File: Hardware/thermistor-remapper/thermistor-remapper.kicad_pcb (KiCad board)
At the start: 2 copper layers, 40 x 56.5 mm, 31 parts, among them Q1 2N7002, Q2 2N7002, Q3 2N7002, Q4 2N7002, Q5 2N7002, Q6 2N7002, Q7 2N7002, U1 MX8500-8.5-04P-BK01-CU-S-A, U2 XL1509-5.0E1

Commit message: Completed prototype
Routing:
- net VDD: track 21.3 -> 53.6 mm, vias 0 -> 1
- net BIT1: track 0.00 -> 8.69 mm
- net BIT2: track 0.00 -> 8.26 mm
- net BIT3: track 0.00 -> 7.51 mm
- net BIT4: track 0.00 -> 6.90 mm
- net BIT5: track 0.00 -> 6.60 mm
- net BIT6: track 0.00 -> 6.41 mm
- net BIT7: track 0.00 -> 6.22 mm
- added copper zone on B.Cu, net GND
- added copper zone on F.Cu, net GND
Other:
- board size 40 x 56.5 mm -> 40 x 57 mm

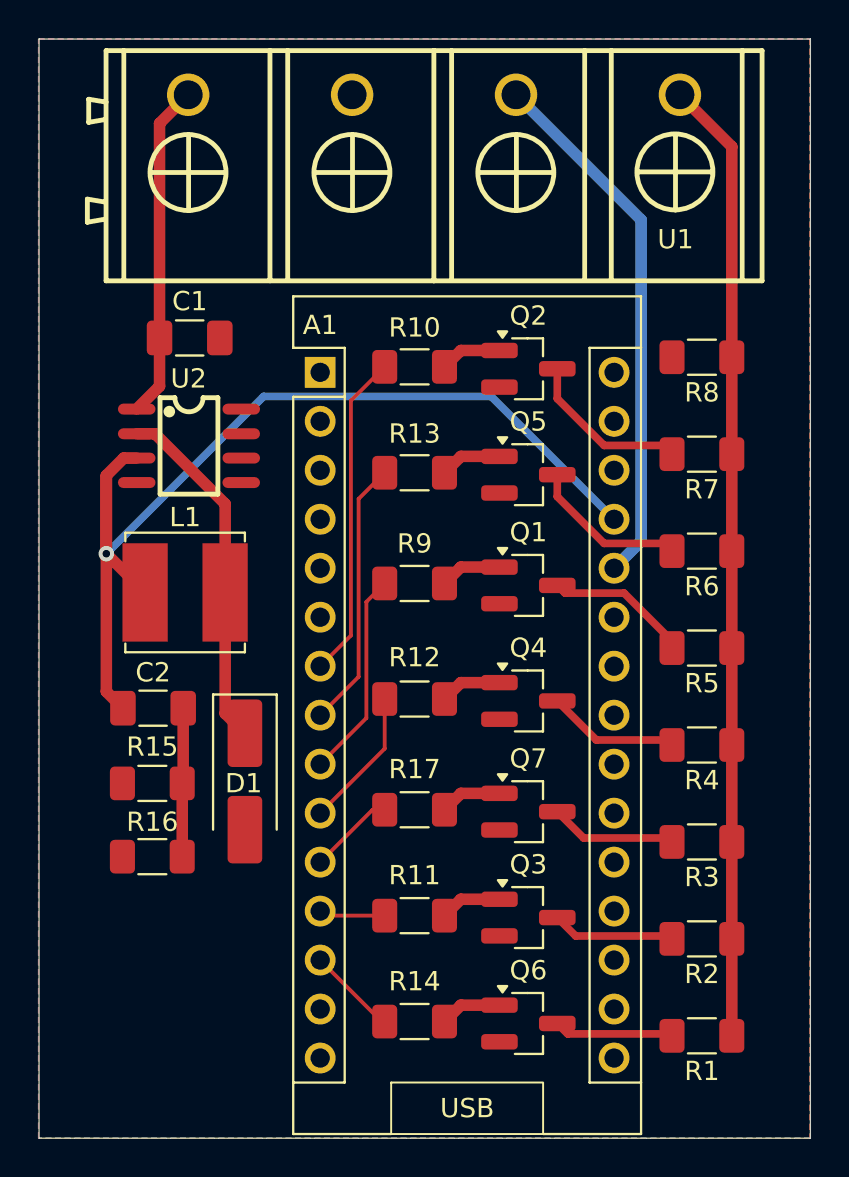
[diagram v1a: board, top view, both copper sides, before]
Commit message: Change resistors to 0806
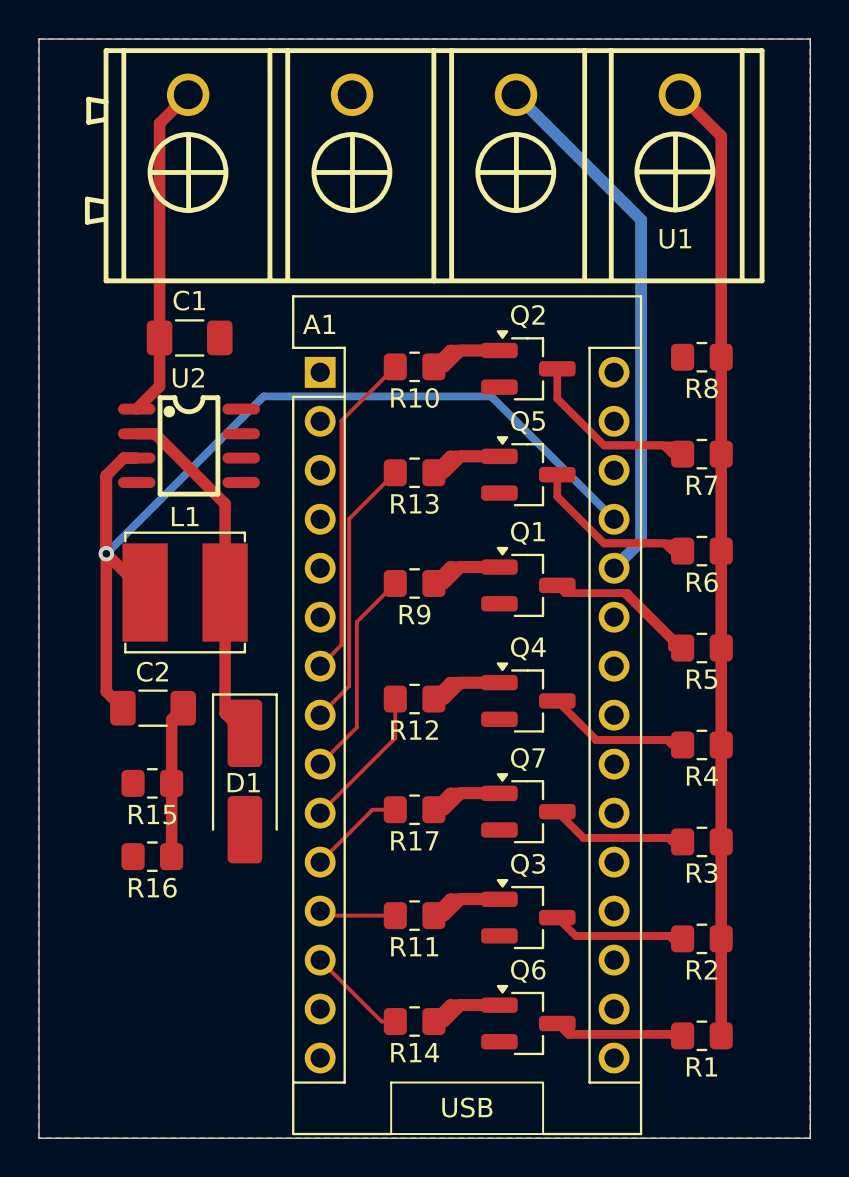
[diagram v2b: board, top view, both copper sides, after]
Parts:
- R1, R10, R11, R12, R13, R14, R15, R16, R17, R2, R3, R4, R5, R6, R7, R8, R9: footprint Resistor_SMD:R_1206_3216Metric_Pad1.30x1.75mm_HandSolder -> Resistor_SMD:R_0805_2012Metric_Pad1.20x1.40mm_HandSolder
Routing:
- net BIT7: track 6.22 -> 13.0 mm
- net BIT6: track 6.41 -> 12.0 mm
- net BIT5: track 6.60 -> 11.8 mm
- net BIT4: track 6.90 -> 11.5 mm
- net BIT3: track 7.51 -> 12.0 mm
- net BIT1: track 8.69 -> 13.0 mm
- net BIT2: track 8.26 -> 12.5 mm
- net Net-(Q6-G): track 3.20 -> 6.95 mm
- net Net-(Q5-G): track 3.20 -> 6.95 mm
- net Net-(Q1-G): track 3.20 -> 6.95 mm
- net Net-(Q3-G): track 3.20 -> 6.95 mm
- net Net-(Q2-G): track 3.20 -> 6.95 mm
- net Net-(Q7-G): track 3.20 -> 6.95 mm
- net Net-(Q4-G): track 3.20 -> 6.95 mm
- net MCU-D9: track 3.44 -> 3.99 mm
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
